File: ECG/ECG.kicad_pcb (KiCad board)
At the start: 4 copper layers, 81.3 x 109.2 mm, 64 parts, among them J1 Conn_01x03, J2 Conn_01x03, J3 Conn_01x15, J4 Conn_01x15, J5 Conn_01x02, J6 Conn_01x02, J7 Conn_01x02, Q1 DMG2301L, Q2 T2N7002AK, Q3 T2N7002AK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

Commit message: V1.0 candidate
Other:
- board text added: "DC 3-WIRE"
- board text removed: "3-WIRE DC"
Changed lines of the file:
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@@
 			(at 0 -2.5 90)
 			(layer "F.SilkS")
+			(hide yes)
 			(effects
 				(font
@@
 			)
 		)
+		(model "/Users/d66317d/Code/Boards/ECG/Library/3d/691137710002.step"
+			(offset
+				(xyz 5 4 0)
+			)
+			(scale
+				(xyz 1 1 1)
+			)
+			(rotate
+				(xyz -90 -0 -90)
+			)
+		)
 	)
 	(footprint "Resistor_THT:R_Axial_DIN0207_L6.3mm_D2.5mm_P2.54mm_Vertical"
@@
 			(at 0 -2.5 90)
 			(layer "F.SilkS")
+			(hide yes)
 			(effects
 				(font
@@
 	)
 	(gr_text "3-WIRE"
-		(at 139.090001 105.792999 90)
+		(at 135.255 100.965 0)
 		(layer "F.SilkS")
 		(effects
@@
 	)
 	(gr_text "RLD"
-		(at 162.590001 110.542999 90)
+		(at 156.845 107.315 0)
 		(layer "F.SilkS")
 		(effects
@@
 		)
 	)
-	(gr_text "3-WIRE\nDC"
+	(gr_text "DC\n3-WIRE\n"
 		(at 121.6 74.8 0)
 		(layer "F.SilkS")
@@
 	)
 	(gr_text "LEFT"
-		(at 107.6 106.5 0)
+		(at 107.95 107.315 0)
 		(layer "F.SilkS")
 		(effects
@@
 	)
 	(gr_text "SW"
-		(at 128.840001 94.292999 90)
+		(at 127 93.345 0)
 		(layer "F.SilkS")
 		(effects
@@
 	)
 	(gr_text "RIGHT"
-		(at 137.340001 110.542999 90)
+		(at 131.445 107.315 0)
 		(layer "F.SilkS")
 		(effects
@@
 		(effects
 			(font
-				(size 1.5 1.5)
-				(thickness 0.3)
-				(bold yes)
+				(size 1 1)
+				(thickness 0.15)
 			)
 			(justify left bottom)
@@
 	)
 	(gr_text "2-WIRE"
-		(at 133.840001 105.792999 90)
+		(at 130.81 95.885 0)
 		(layer "F.SilkS")
 		(effects
@@
 	)
 	(gr_text "+9V"
-		(at 169.291 74.168 180)
+		(at 163.322 75.438 0)
 		(layer "F.Paste")
 		(effects

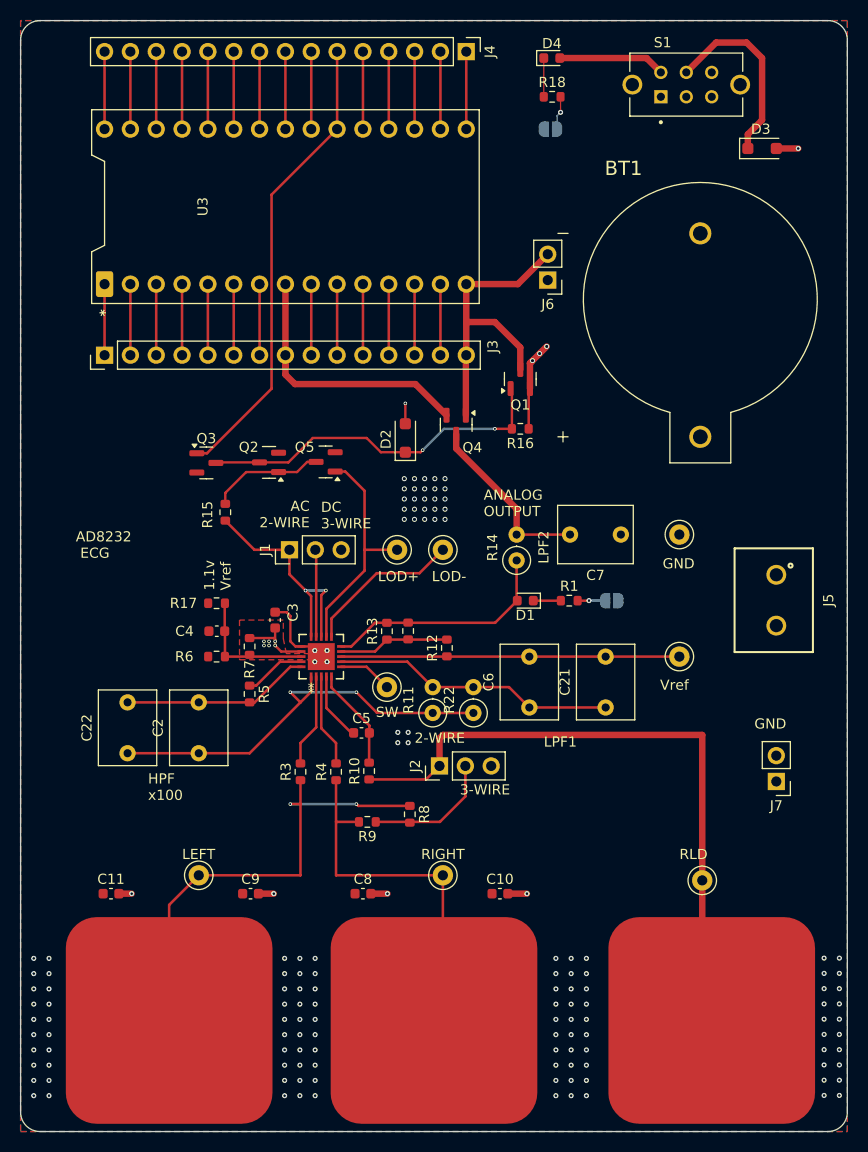
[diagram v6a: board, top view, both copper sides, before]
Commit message: getting close.  Larger vias for cheaper process
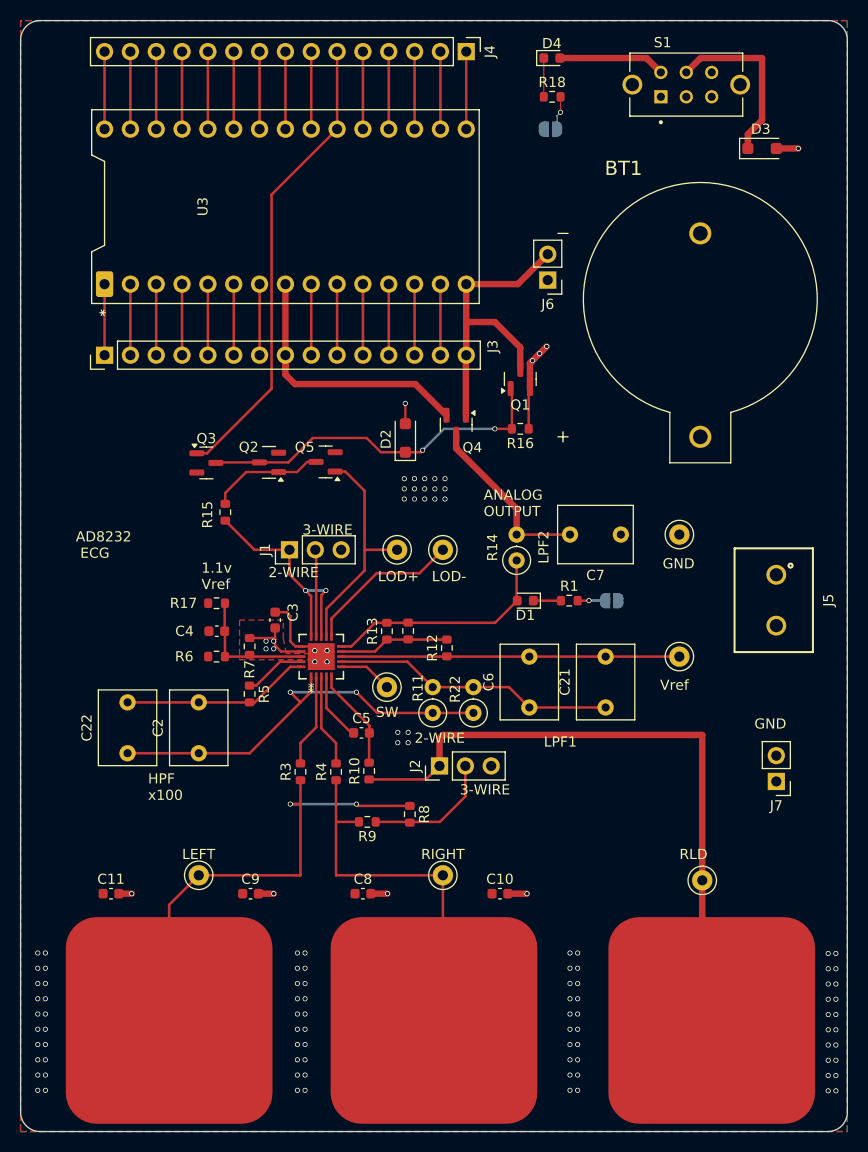
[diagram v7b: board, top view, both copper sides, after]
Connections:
- net Net-(BT1-Pad+) renamed /BPLUS
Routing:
- net /BPLUS: track 35.3 -> 0.00 mm
- net +3V0: track 37.1 -> 38.7 mm, vias 12 -> 10
- net Net-(D3-K): track 18.8 -> 17.5 mm
- net GND: vias 133 -> 103
- added copper zone on In2.Cu, net /BPLUS
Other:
- board text removed: "AC 2-WIRE"
- board text removed: "DC 3-WIRE"

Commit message: Edits from review with Kofi
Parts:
- removed D2: 1N4148, Diode_SMD:D_SOD-123F
- added C1: 100nF, Capacitor_SMD:C_0603_1608Metric, F.Cu at (144.0, 40.1)
- added C12: 100nF, Capacitor_SMD:C_0603_1608Metric, F.Cu at (144.0, 43.3)
- added C13: 100nF, Capacitor_SMD:C_0603_1608Metric, F.Cu at (97.8, 63.3)
- added C14: 100nF, Capacitor_SMD:C_0603_1608Metric, F.Cu at (97.8, 65.8)
- added J8: Conn_01x02, Connector_PinHeader_2.54mm:PinHeader_1x02_P2.54mm_Vertical, F.Cu at (102.9, 65.0)
- D1: value LED -> LED_Red
- TP9: footprint ECG_Footprints:FingerPad -> ECG_Footprints:RefPad
- moved TP9 8.26 mm to (160.0, 131.3)
- moved D1 0.15 mm to (141.6, 81.9)
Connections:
- D4 pad 2: +9V -> /VIN
- J4 pad 5: /D2 -> /LEADS_ON
- Q2 pad 1: /PWR_ON -> /LEADS_ON
- Q5 pad 3: /PWR_ON -> /LEADS_ON
- R15 pad 2: /PWR_ON -> /LEADS_ON
- U3 pad 20: /D2 -> /LEADS_ON
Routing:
- net /LEADS_ON: track 0.00 -> 56.6 mm, vias 0 -> 1
- net /D2: track 38.3 -> 0.00 mm, vias 1 -> 0
- net /VIN: track 30.6 -> 46.6 mm, vias 0 -> 8
- net /PWR_ON: track 11.3 -> 0.00 mm
- net /PWR_OFF_HV: track 35.7 -> 46.9 mm
- net +9V: track 58.4 -> 47.8 mm
- added copper zone on In2.Cu, net /VIN
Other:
- board text added: "Arduino OFF (9V)"
